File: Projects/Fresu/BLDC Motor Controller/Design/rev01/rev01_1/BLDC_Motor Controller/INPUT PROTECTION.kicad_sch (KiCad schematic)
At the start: 0 parts

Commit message: UPDATE 11
INPUT PROTECTION SCHEMATIC COMPLETE
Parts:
- added C59, C60: LKMI2501K821MF, symbol Device:C_Polarized_Small_US
- added C61, C62: 100n, symbol Device:C
- added D13: SMAJ60CA, Diode_SMD:D_SMA, symbol Diode:SMAJ60CA
- added D14: LED_G, symbol Device:LED
- added J10: XH-2PWBPZ, symbol Connector_Generic:Conn_01x02
- added J9: XT60PW-M, symbol Connector_Generic:Conn_01x02
- added R52, R54: 39k, symbol Device:R
- added R53, R55: 2k2, symbol Device:R
- added TH2: 10k, symbol Device:Thermistor_NTC
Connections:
- new net: D14.2 (A), R54.2
- new net +3V3: C62.1, R55.1
- new net +VDC: C59.1, C60.1, D13.2 (A2), J9.2 (Pin_2), R52.1, R54.1
- new net ADC_TEMP: J10.2 (Pin_2), R55.2, TH2.1
- new net AN_IN: C61.1, R52.2, R53.1
- new net GND: C59.2, C60.2, C61.2, C62.2, D13.1 (A1), D14.1 (K), J10.1 (Pin_1), J9.1 (Pin_1), R53.2, TH2.2
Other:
- note added: "FEEDBACK MCU"
- note added: "INPUT PROTECTION"
- note added: "WHEN: VDC = 60V => AN_IN = 3V204"
- note removed: "0-60V"
- note removed: "BLOCK DIAGRAM"
- note removed: "CAN"
- note removed: "COM"
- note removed: "HALL/ENCODER"
- note removed: "MCU"
- note removed: "MOSFET"
- note removed: "MOSFET DRIVER"
- note removed: "MOTOR"
- note removed: "SERVO"
- note removed: "TEMP_SENSOR"
- note removed: "USB"
- note removed: "V_SUPPLY"

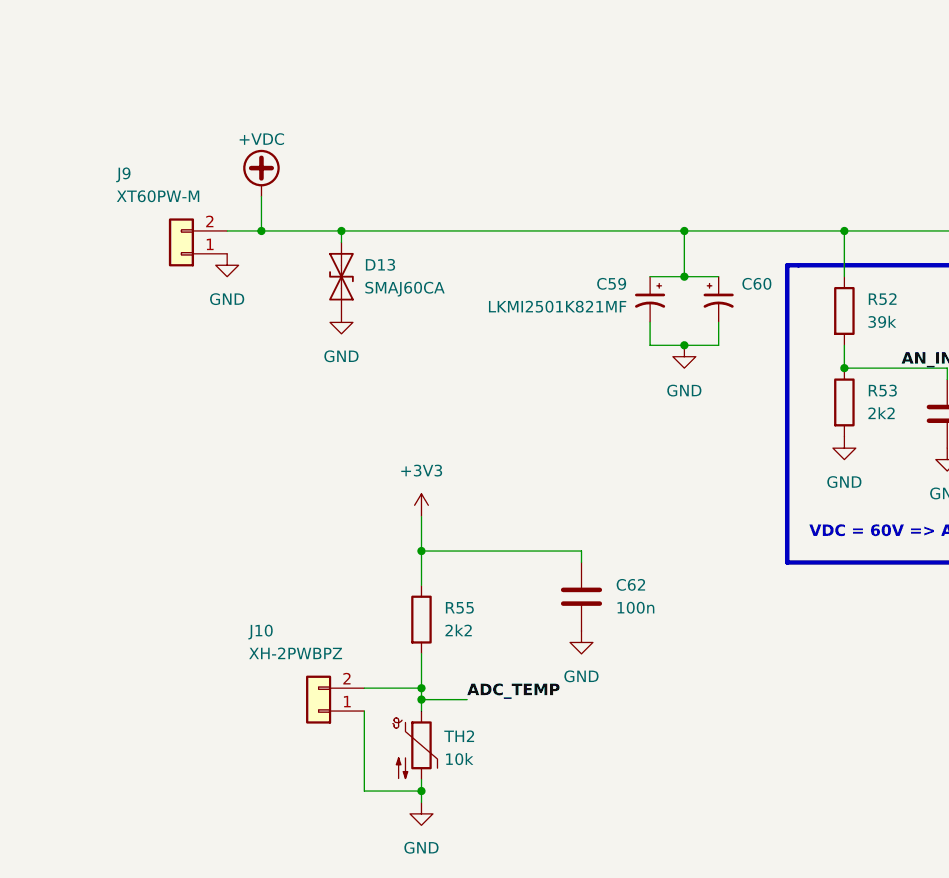
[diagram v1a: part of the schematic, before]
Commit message: Update 13
Added:
1) USB Schematic
2) footprints to all parts
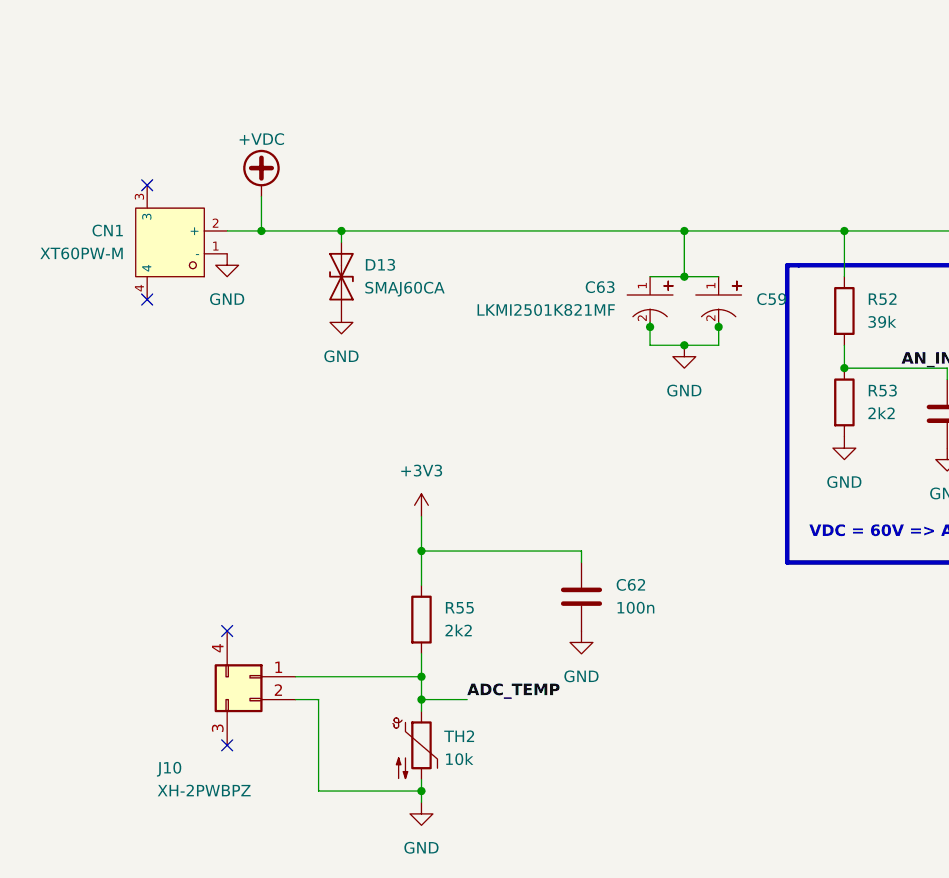
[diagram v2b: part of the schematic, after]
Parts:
- removed C59, C60: LKMI2501K821MF, symbol Device:C_Polarized_Small_US
- removed J9: XT60PW-M, symbol Connector_Generic:Conn_01x02
- added C59, C63: LKMI2501K821MF, DF_ESC_Footprint_Library:CAP-TH_BD18.0-P7.50-D1.2-SIDE, symbol DF_ESC_Symbol_Library:LKMI2501K821MF
- added CN1: XT60PW-M, DF_ESC_Footprint_Library:CONN-TH_XT60PW-M, symbol DF_ESC_Symbol_Library:XT60PW-M
- C61, C62: footprint (none) -> Capacitor_SMD:C_0603_1608Metric
- D14: footprint (none) -> LED_SMD:LED_1206_3216Metric
- J10: footprint (none) -> DF_ESC_Footprint_Library:CONN-SMD_XH-2PWBPZ
- R52, R53, R54, R55, TH2: footprint (none) -> Resistor_SMD:R_0603_1608Metric_Pad0.98x0.95mm_HandSolder
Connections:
- net +VDC: now also C59.1, C63.1, CN1.2 (+)
- net ADC_TEMP: now also J10.1 (Pin_1); no longer J10.2 (Pin_2)
- net GND: now also J10.2 (Pin_2), C59.2, C63.2, CN1.1 (-); no longer J10.1 (Pin_1)
- no-connect marks 0 -> 4

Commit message: Update 15
Fixing some schematic errors

initial layout of larger component complete
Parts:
- renumbered C62 to C55, C63 to C56, C59 to C57, C61 to C58, D13 to D10, D14 to D11, J10 to J8, R52 to R56, R53 to R57, R54 to R58

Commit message: Update 17
Started laying out the driver and the main FET power polygons
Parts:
- added C12: LKMI2501K821MF, DF_ESC_Footprint_Library:CAP-TH_BD18.0-P7.50-D1.2-SIDE, symbol DF_ESC_Symbol_Library:LKMI2501K821MF
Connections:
- net +VDC: now also C12.1
- net GND: now also C12.2
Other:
- moved on the sheet: C56, C57, D10

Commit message: Update 26
Matched DF's Designators to mine so I can use BOM as is

Updated MFR'ing files

Rev1 Ready for release
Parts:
- renumbered C56 to C1, C58 to C2, C55 to C22, C57 to C58, C12 to C99, D10 to D1, D11 to D2, CN1 to J1, R56 to R1, R55 to R11, R57 to R2, R58 to R3, TH2 to TH1, J8 to U5
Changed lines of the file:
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@@
 		(dnp no)
 		(fields_autoplaced yes)
-		(property "Reference" "R55"
-			(at 102.87 105.41 0)
+		(property "Reference" "R11"
+			(at 102.87 105.4099 0)
 			(effects
 				(font
@@
 		)
 		(property "Value" "2k2"
-			(at 102.87 107.95 0)
+			(at 102.87 107.9499 0)
 			(effects
 				(font
@@
 			(project "BLDC_Motor Controller"
 				(path "/e63e39d7-6ac0-4ffd-8aa3-1841a4541b55/0a58613e-bda0-4563-bf79-2ea6a0b26c8f"
-					(reference "R55")
+					(reference "R11")
 					(unit 1)
 				)
@@
 		(dnp no)
 		(fields_autoplaced yes)
-		(property "Reference" "R56"
-			(at 149.86 71.12 0)
+		(property "Reference" "R1"
+			(at 149.86 71.1199 0)
 			(effects
 				(font
@@
 		)
 		(property "Value" "39k"
-			(at 149.86 73.66 0)
+			(at 149.86 73.6599 0)
 			(effects
 				(font
@@
 			(project "BLDC_Motor Controller"
 				(path "/e63e39d7-6ac0-4ffd-8aa3-1841a4541b55/0a58613e-bda0-4563-bf79-2ea6a0b26c8f"
-					(reference "R56")
+					(reference "R1")
 					(unit 1)
 				)
@@
 		(dnp no)
 		(fields_autoplaced yes)
-		(property "Reference" "TH2"
-			(at 102.87 119.6975 0)
+		(property "Reference" "TH1"
+			(at 102.87 119.6974 0)
 			(effects
 				(font
@@
 		)
 		(property "Value" "10k"
-			(at 102.87 122.2375 0)
+			(at 102.87 122.2374 0)
 			(effects
 				(font
@@
 			(project "BLDC_Motor Controller"
 				(path "/e63e39d7-6ac0-4ffd-8aa3-1841a4541b55/0a58613e-bda0-4563-bf79-2ea6a0b26c8f"
-					(reference "TH2")
+					(reference "TH1")
 					(unit 1)
 				)
@@
 		(dnp no)
 		(fields_autoplaced yes)
-		(property "Reference" "R58"
-			(at 176.53 66.04 0)
-			(effects
-				(font
-					(size 1.27 1.27)
-				)
-				(justify left)
+		(property "Reference" "R3"
+			(at 181.61 66.0399 0)
+			(effects
+				(font
+					(size 1.27 1.27)
+				)
+				(justify right)
 			)
 		)
 		(property "Value" "39k"
-			(at 176.53 68.58 0)
-			(effects
-				(font
-					(size 1.27 1.27)
-				)
-				(justify left)
+			(at 181.61 68.5799 0)
+			(effects
+				(font
+					(size 1.27 1.27)
+				)
+				(justify right)
 			)
 		)
@@
 			(project "BLDC_Motor Controller"
 				(path "/e63e39d7-6ac0-4ffd-8aa3-1841a4541b55/0a58613e-bda0-4563-bf79-2ea6a0b26c8f"
-					(reference "R58")
+					(reference "R3")
 					(unit 1)
 				)
@@
 		(on_board yes)
 		(dnp no)
-		(property "Reference" "C56"
+		(property "Reference" "C1"
 			(at 118.11 64.77 0)
 			(effects
@@
 			(project "BLDC_Motor Controller"
 				(path "/e63e39d7-6ac0-4ffd-8aa3-1841a4541b55/0a58613e-bda0-4563-bf79-2ea6a0b26c8f"
-					(reference "C56")
+					(reference "C1")
 					(unit 1)
 				)
@@
 		(on_board yes)
 		(dnp no)
-		(property "Reference" "D11"
+		(property "Reference" "D2"
 			(at 182.88 77.7875 90)
 			(effects
@@
 			(project "BLDC_Motor Controller"
 				(path "/e63e39d7-6ac0-4ffd-8aa3-1841a4541b55/0a58613e-bda0-4563-bf79-2ea6a0b26c8f"
-					(reference "D11")
+					(reference "D2")
 					(unit 1)
 				)
@@
 		(dnp no)
 		(fields_autoplaced yes)
-		(property "Reference" "CN1"
-			(at 67.31 63.5 0)
+		(property "Reference" "J1"
+			(at 67.31 63.4999 0)
 			(effects
 				(font
@@
 		)
 		(property "Value" "XT60PW-M"
-			(at 67.31 66.04 0)
+			(at 67.31 66.0399 0)
 			(effects
 				(font
@@
 			(project "BLDC_Motor Controller"
 				(path "/e63e39d7-6ac0-4ffd-8aa3-1841a4541b55/0a58613e-bda0-4563-bf79-2ea6a0b26c8f"
-					(reference "CN1")
+					(reference "J1")
 					(unit 1)
 				)
@@
 		(dnp no)
 		(fields_autoplaced yes)
-		(property "Reference" "D10"
-			(at 90.17 67.31 90)
+		(property "Reference" "D1"
+			(at 90.17 67.3099 90)
 			(effects
 				(font
@@
 		)
 		(property "Value" "SMAJ60CA"
-			(at 90.17 69.85 90)
+			(at 90.17 69.8499 90)
 			(effects
 				(font
@@
 			(project "BLDC_Motor Controller"
 				(path "/e63e39d7-6ac0-4ffd-8aa3-1841a4541b55/0a58613e-bda0-4563-bf79-2ea6a0b26c8f"
-					(reference "D10")
+					(reference "D1")
 					(unit 1)
 				)
@@
 		(dnp no)
 		(fields_autoplaced yes)
-		(property "Reference" "C55"
-			(at 121.92 102.87 0)
+		(property "Reference" "C22"
+			(at 121.92 102.8699 0)
 			(effects
 				(font
@@
 		)
 		(property "Value" "100n"
-			(at 121.92 105.41 0)
+			(at 121.92 105.4099 0)
 			(effects
 				(font
@@
 			(project "BLDC_Motor Controller"
 				(path "/e63e39d7-6ac0-4ffd-8aa3-1841a4541b55/0a58613e-bda0-4563-bf79-2ea6a0b26c8f"
-					(reference "C55")
+					(reference "C22")
 					(unit 1)
 				)
@@
 		(dnp no)
 		(fields_autoplaced yes)
-		(property "Reference" "R57"
-			(at 149.86 81.28 0)
+		(property "Reference" "R2"
+			(at 149.86 81.2799 0)
 			(effects
 				(font
@@
 		)
 		(property "Value" "2k2"
-			(at 149.86 83.82 0)
+			(at 149.86 83.8199 0)
 			(effects
 				(font
@@
 			(project "BLDC_Motor Controller"
 				(path "/e63e39d7-6ac0-4ffd-8aa3-1841a4541b55/0a58613e-bda0-4563-bf79-2ea6a0b26c8f"
-					(reference "R57")
+					(reference "R2")
 					(unit 1)
 				)
@@
 		(on_board yes)
 		(dnp no)
-		(property "Reference" "J8"
+		(property "Reference" "U5"
 			(at 72.39 123.19 0)
 			(effects
@@
 			(project "BLDC_Motor Controller"
 				(path "/e63e39d7-6ac0-4ffd-8aa3-1841a4541b55/0a58613e-bda0-4563-bf79-2ea6a0b26c8f"
-					(reference "J8")
+					(reference "U5")
 					(unit 1)
 				)
@@
 		(on_board yes)
 		(dnp no)
-		(property "Reference" "C12"
+		(property "Reference" "C99"
 			(at 132.08 67.31 0)
 			(effects
@@
 			(project "BLDC_Motor Controller"
 				(path "/e63e39d7-6ac0-4ffd-8aa3-1841a4541b55/0a58613e-bda0-4563-bf79-2ea6a0b26c8f"
-					(reference "C12")
+					(reference "C99")
 					(unit 1)
 				)
@@
 		(on_board yes)
 		(dnp no)
-		(property "Reference" "C57"
+		(property "Reference" "C58"
 			(at 127 67.31 0)
 			(effects
@@
 			(project "BLDC_Motor Controller"
 				(path "/e63e39d7-6ac0-4ffd-8aa3-1841a4541b55/0a58613e-bda0-4563-bf79-2ea6a0b26c8f"
-					(reference "C57")
+					(reference "C58")
 					(unit 1)
 				)
@@
 		(dnp no)
 		(fields_autoplaced yes)
-		(property "Reference" "C58"
-			(at 162.56 82.55 0)
+		(property "Reference" "C2"
+			(at 162.56 82.5499 0)
 			(effects
 				(font
@@
 		)
 		(property "Value" "100n"
-			(at 162.56 85.09 0)
+			(at 162.56 85.0899 0)
 			(effects
 				(font
@@
 			(project "BLDC_Motor Controller"
 				(path "/e63e39d7-6ac0-4ffd-8aa3-1841a4541b55/0a58613e-bda0-4563-bf79-2ea6a0b26c8f"
-					(reference "C58")
-					(unit 1)
-				)
+					(reference "C2")
+					(unit 1)
+				)
